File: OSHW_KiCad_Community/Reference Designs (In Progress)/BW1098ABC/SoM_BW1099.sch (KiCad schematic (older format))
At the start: 25 parts, among them J1 20021121-00010T1LF, J2 20021121-00010T1LF, J3 DF40HC(3.0)-100DS-0.4V_BW1099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, J4 20021121-00010T1LF, Q1 RE1C002UNTCL, Q2 RE1C002UNTCL, Q3 RE1C002UNTCL

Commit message: edits to abc
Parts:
- D1: value RED0603 -> RED
- D2, D3: value ORANGE0603 -> ORANGE
- R1, R2, R3, R4: value 1k 0402 -> 1k
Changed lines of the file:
@@
 AR Path="/5FF8D9B2/6009EFFA" Ref="D3"  Part="1"
 F 0 "D3" V 1939 7632 50  0000 R CNN
-F 1 "ORANGE0603" V 1848 7632 50  0000 R CNN
+F 1 "ORANGE" V 1848 7632 50  0000 R CNN
 F 2 "Diode_SMD:D_0603_1608Metric" H 1900 7750 50  0001 C CNN
 F 3 "~" H 1900 7750 50  0001 C CNN
@@
 AR Path="/5FF8D9B2/6009F000" Ref="R4"  Part="1"
 F 0 "R4" H 1968 7396 50  0000 L CNN
-F 1 "1k 0402" H 1968 7305 50  0000 L CNN
+F 1 "1k " H 1968 7305 50  0000 L CNN
 F 2 "Resistor_SMD:R_0402_1005Metric" H 1900 7350 50  0001 C CNN
 F 3 "~" H 1900 7350 50  0001 C CNN
@@
 AR Path="/5FF8D9B2/6009F015" Ref="D2"  Part="1"
 F 0 "D2" V 1889 5782 50  0000 R CNN
-F 1 "ORANGE0603" V 1798 5782 50  0000 R CNN
+F 1 "ORANGE" V 1798 5782 50  0000 R CNN
 F 2 "Diode_SMD:D_0603_1608Metric" H 1850 5900 50  0001 C CNN
 F 3 "~" H 1850 5900 50  0001 C CNN
@@
 AR Path="/5FF8D9B2/6009F01B" Ref="R3"  Part="1"
 F 0 "R3" H 1918 5546 50  0000 L CNN
-F 1 "1k 0402" H 1918 5455 50  0000 L CNN
+F 1 "1k" H 1918 5455 50  0000 L CNN
 F 2 "Resistor_SMD:R_0402_1005Metric" H 1850 5500 50  0001 C CNN
 F 3 "~" H 1850 5500 50  0001 C CNN
@@
 AR Path="/5FF8D9B2/6009F030" Ref="D1"  Part="1"
 F 0 "D1" V 1889 3482 50  0000 R CNN
-F 1 "RED0603" V 1798 3482 50  0000 R CNN
+F 1 "RED" V 1798 3482 50  0000 R CNN
 F 2 "Diode_SMD:D_0603_1608Metric" H 1850 3600 50  0001 C CNN
 F 3 "~" H 1850 3600 50  0001 C CNN
@@
 AR Path="/5FF8D9B2/6009F036" Ref="R2"  Part="1"
 F 0 "R2" H 1918 3246 50  0000 L CNN
-F 1 "1k 0402" H 1918 3155 50  0000 L CNN
+F 1 "1k" H 1918 3155 50  0000 L CNN
 F 2 "Resistor_SMD:R_0402_1005Metric" H 1850 3200 50  0001 C CNN
 F 3 "~" H 1850 3200 50  0001 C CNN
@@
 AR Path="/5FF8D9B2/6009F045" Ref="R1"  Part="1"
 F 0 "R1" H 1418 3146 50  0000 L CNN
-F 1 "1k 0402" H 1418 3055 50  0000 L CNN
+F 1 "1k" H 1418 3055 50  0000 L CNN
 F 2 "Resistor_SMD:R_0402_1005Metric" H 1350 3100 50  0001 C CNN
 F 3 "~" H 1350 3100 50  0001 C CNN

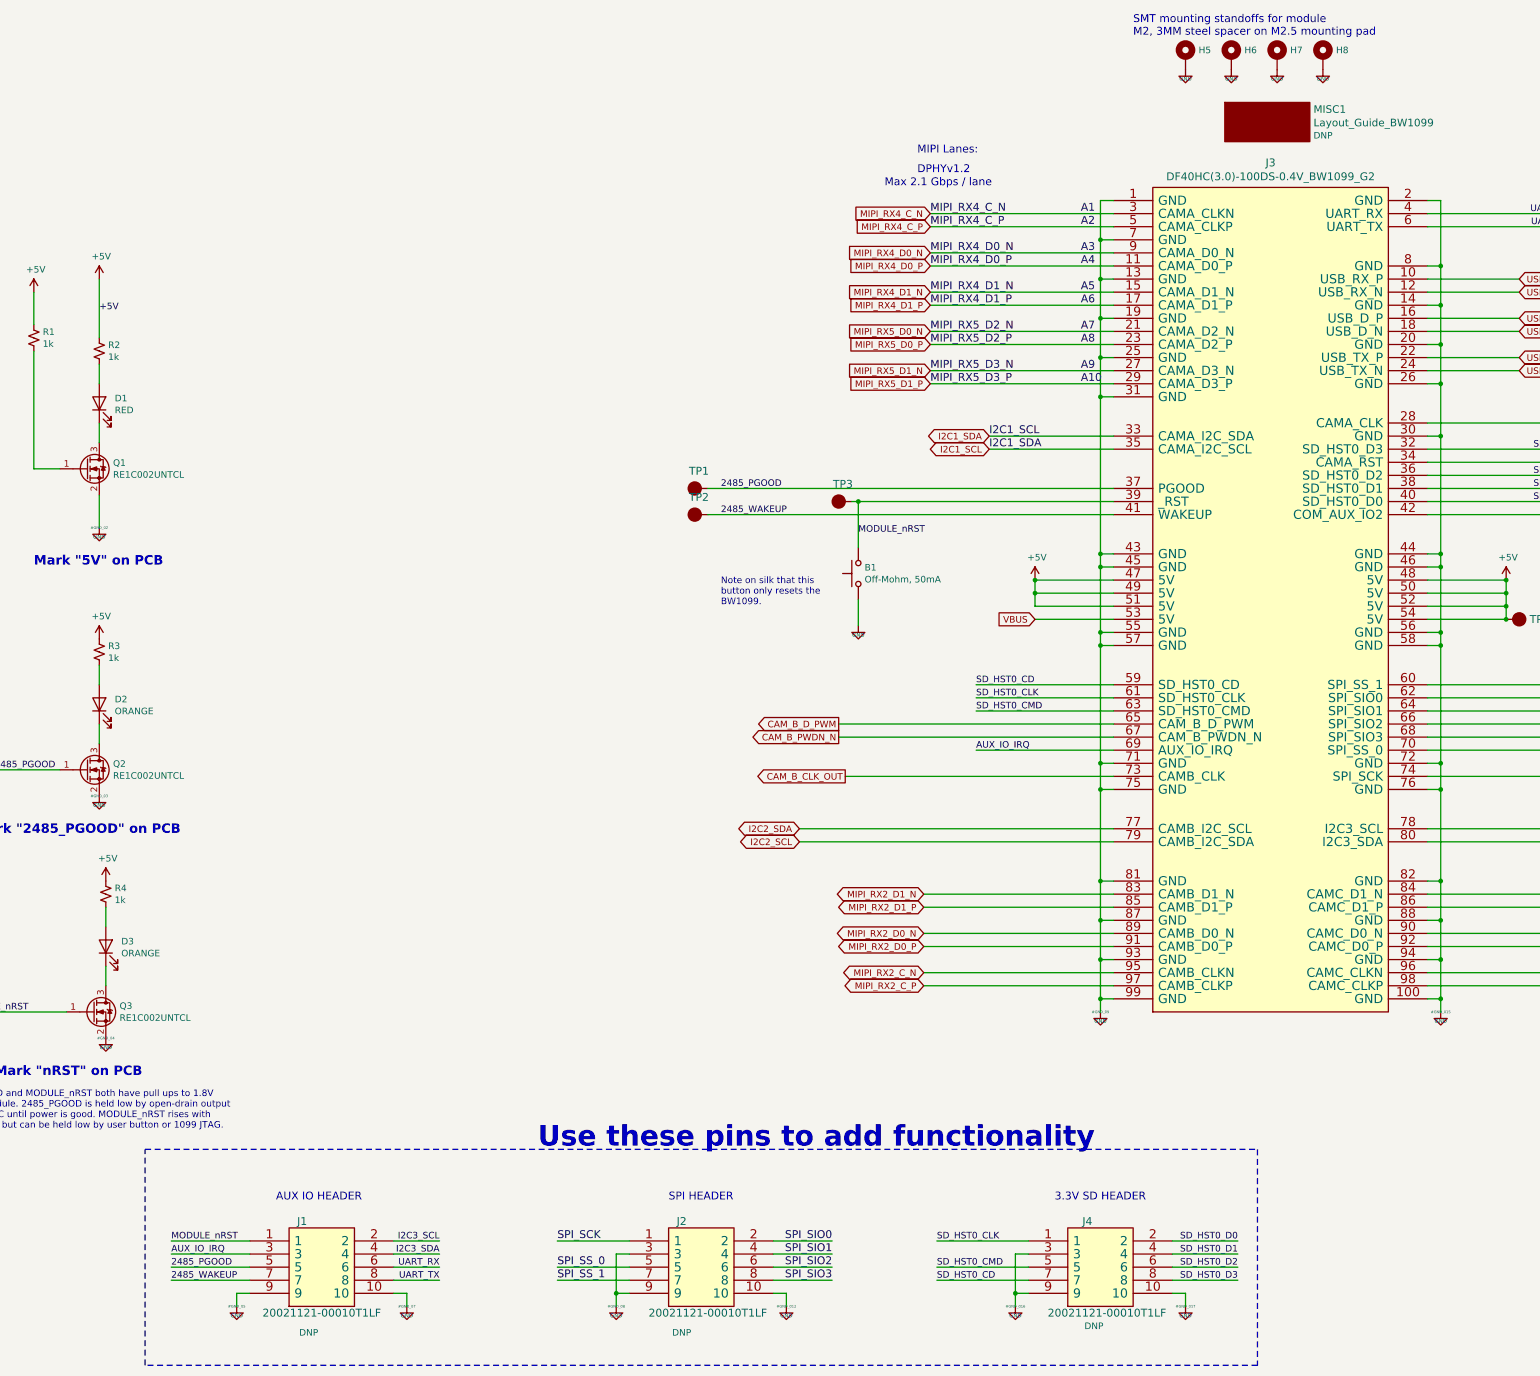
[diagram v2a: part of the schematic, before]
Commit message: added module mounts and started layout for abc
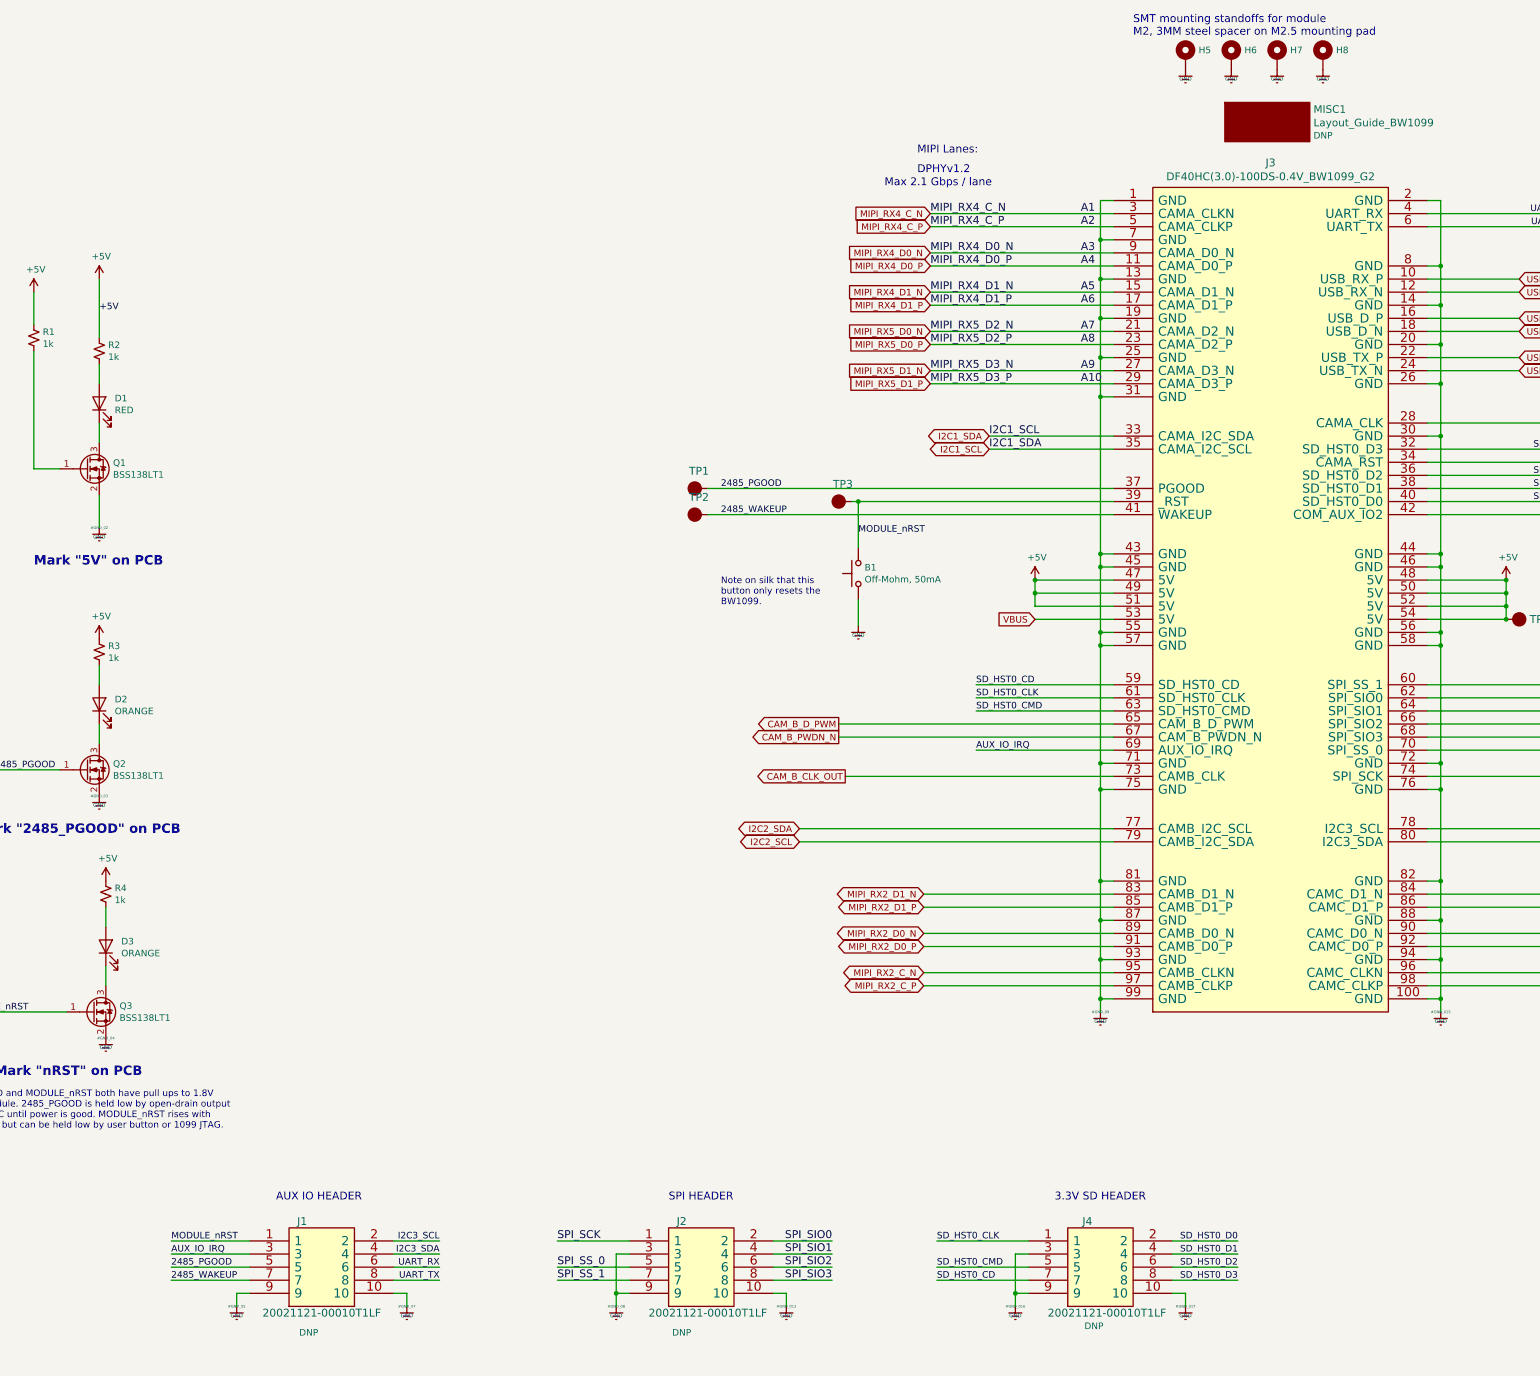
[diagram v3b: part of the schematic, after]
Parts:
- B1: footprint Luxonis_Kicad_Master:DTSM32NVTR -> Luxonis_KiCad_Master:DTSM32NVTR
- J3: footprint Luxonis_Kicad_Master:DF40HC(3.0)-100DS-0.4V(58) -> Luxonis_KiCad_Master:DF40HC(3.0)-100DS-0.4V(58)
- MISC1: footprint Luxonis_Kicad_Master:BW1099_Layout_Guide -> Luxonis_KiCad_Master:BW1099_Layout_Guide
- Q1, Q2, Q3: value RE1C002UNTCL -> BSS138LT1; footprint (none) -> Package_TO_SOT_SMD:SOT-23
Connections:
- net GND renamed Earth
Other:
- note removed: "Use these pins to add functionality"
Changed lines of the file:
@@
 $EndDescr
 $Comp
-L power:GND #GND_?
+L power:Earth #GND_?
 U 1 1 6009EE60
 P 12100 8250
@@
 SMT mounting standoffs for module\nM2, 3MM steel spacer on M2.5 mounting pad
 $Comp
-L power:GND #GND_?
+L power:Earth #GND_?
 U 1 1 6009EE67
 P 7650 5300
@@
 $EndComp
 $Comp
-L power:GND #GND_?
+L power:Earth #GND_?
 U 1 1 6009EE6D
 P 11200 1050
@@
 SPI_SIO3
 $Comp
-L power:GND #GND_?
+L power:Earth #GND_?
 U 1 1 6009EE7D
 P 4200 10500
@@
 $EndComp
 $Comp
-L power:GND #GND_?
+L power:Earth #GND_?
 U 1 1 6009EE83
 P 9500 8250
@@
 Mark "nRST" on PCB
 $Comp
-L power:GND #GND_?
+L power:Earth #GND_?
 U 1 1 6009EE8C
 P 1900 8450
@@
 $EndComp
 $Comp
-L power:GND #GND_?
+L power:Earth #GND_?
 U 1 1 6009EE92
 P 2900 10500
@@
 $EndComp
 $Comp
-L power:GND #GND_?
+L power:Earth #GND_?
 U 1 1 6009EE98
 P 5800 10500
@@
 $EndComp
 $Comp
-L power:GND #GND_?
+L power:Earth #GND_?
 U 1 1 6009EE9E
 P 7100 10500
@@
 $EndComp
 $Comp
-L power:GND #GND_?
+L power:Earth #GND_?
 U 1 1 6009EEA4
 P 8850 10500
@@
 $EndComp
 $Comp
-L power:GND #GND_?
+L power:Earth #GND_?
 U 1 1 6009EEAA
 P 10150 10500
@@
 $EndComp
 $Comp
-L power:GND #GND_?
+L power:Earth #GND_?
 U 1 1 6009EF80
 P 10850 1050
@@
 $EndComp
 $Comp
-L power:GND #GND_?
+L power:Earth #GND_?
 U 1 1 6009EF86
 P 10500 1050
@@
 $EndComp
 $Comp
-L power:GND #GND_?
+L power:Earth #GND_?
 U 1 1 6009EF8C
 P 10150 1050
@@
 F 0 "B1" V 7696 4852 50  0000 R CNN
 F 1 "Off-Mohm, 50mA" V 7605 4852 50  0000 R CNN
-F 2 "Luxonis_Kicad_Master:DTSM32NVTR" H 7650 5100 50  0001 C CNN
+F 2 "Luxonis_KiCad_Master:DTSM32NVTR" H 7650 5100 50  0001 C CNN
 F 3 "http://www.apem.com/int/index.php?controller=attachment&id_attachment=488" H 7650 5100 50  0001 C CNN
 	1    7650 4900
@@
 AR Path="/5FF8D9B2/6009F007" Ref="Q3"  Part="1"
 F 0 "Q3" H 2005 8296 50  0000 L CNN
-F 1 "RE1C002UNTCL" H 2005 8205 50  0000 L CNN
-F 2 "" H 2000 8350 50  0001 C CNN
+F 1 "BSS138LT1" H 2005 8205 50  0000 L CNN
+F 2 "Package_TO_SOT_SMD:SOT-23" H 2000 8350 50  0001 C CNN
 F 3 "~" H 1800 8250 50  0001 C CNN
 	1    1800 8250
@@
 	1900 8050 1900 7900
 $Comp
-L power:GND #GND_?
+L power:Earth #GND_?
 U 1 1 6009F00F
 P 1850 6600
@@
 AR Path="/5FF8D9B2/6009F022" Ref="Q2"  Part="1"
 F 0 "Q2" H 1955 6446 50  0000 L CNN
-F 1 "RE1C002UNTCL" H 1955 6355 50  0000 L CNN
-F 2 "" H 1950 6500 50  0001 C CNN
+F 1 "BSS138LT1" H 1955 6355 50  0000 L CNN
+F 2 "Package_TO_SOT_SMD:SOT-23" H 1950 6500 50  0001 C CNN
 F 3 "~" H 1750 6400 50  0001 C CNN
 	1    1750 6400
@@
 	1850 6200 1850 6050
 $Comp
-L power:GND #GND_?
+L power:Earth #GND_?
 U 1 1 6009F02A
 P 1850 4550
@@
 AR Path="/5FF8D9B2/6009F03D" Ref="Q1"  Part="1"
 F 0 "Q1" H 1955 4146 50  0000 L CNN
-F 1 "RE1C002UNTCL" H 1955 4055 50  0000 L CNN
-F 2 "" H 1950 4200 50  0001 C CNN
+F 1 "BSS138LT1" H 1955 4055 50  0000 L CNN
+F 2 "Package_TO_SOT_SMD:SOT-23" H 1950 4200 50  0001 C CNN
 F 3 "~" H 1750 4100 50  0001 C CNN
 	1    1750 4100
@@
 F 0 "J3" H 10800 2339 60  0000 C CNN
 F 1 "DF40HC(3.0)-100DS-0.4V_BW1099_G2" H 10800 2233 60  0000 C CNN
-F 2 "Luxonis_Kicad_Master:DF40HC(3.0)-100DS-0.4V(58)" H 9600 2050 60  0001 C CNN
+F 2 "Luxonis_KiCad_Master:DF40HC(3.0)-100DS-0.4V(58)" H 9600 2050 60  0001 C CNN
 F 3 "https://www.hirose.com/product/document?clcode=CL0684-4003-3-51&productname=DF40C-60DP-0.4V(51)&series=DF40&documenttype=Catalog&lang=en&documentid=D31649_en" H 9600 2050 60  0001 C CNN
 	1    9600 2050
@@
 F 0 "MISC1" H 11128 1547 58  0000 L CNN
 F 1 "Layout_Guide_BW1099" H 11128 1444 58  0000 L CNN
-F 2 "Luxonis_Kicad_Master:BW1099_Layout_Guide" H 10550 1850 58  0001 C CNN
+F 2 "Luxonis_KiCad_Master:BW1099_Layout_Guide" H 10550 1850 58  0001 C CNN
 F 3 "" H 10550 1850 58  0001 C CNN
 F 4 "DNP" H 11128 1347 50  0000 L CNN "Population"
@@
 Text GLabel 7500 6050 0    50   Output ~ 0
 CAM_B_D_PWM
-Wire Notes Line width 16 style solid rgb(0, 255, 0)
-	10700 10950 2200 10950
-Wire Notes Line width 16 style solid rgb(0, 255, 0)
-	2200 10950 2200 9300
-Wire Notes Line width 16 style solid rgb(0, 255, 0)
-	2200 9300 10700 9300
-Wire Notes Line width 16 style solid rgb(0, 255, 0)
-	10700 9300 10700 10950
-Text Notes 5200 9300 0    157  ~ 31
-Use these pins to add functionality
 $EndSCHEMATC

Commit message: abc board pcb work
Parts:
- removed J1, J4: 20021121-00010T1LF, symbol BW1098ABC-rescue:20021121-00010T1LF-depthAI_sch
- added J1, J4: Conn_02x05_Odd_Even, Connector_PinSocket_2.54mm:PinSocket_2x05_P2.54mm_Vertical, symbol Connector_Generic:Conn_02x05_Odd_Even
- J2: footprint (none) -> Connector_PinHeader_2.54mm:PinHeader_1x02_P2.54mm_Vertical
- R1, R2, R3, R4: footprint Resistor_SMD:R_0402_1005Metric -> Resistor_SMD:R_0603_1608Metric
- TP1, TP2, TP3, TP4, TP5: footprint TestPoint:TestPoint_Loop_D1.80mm_Drill1.0mm_Beaded -> TestPoint:TestPoint_Pad_1.0x1.0mm
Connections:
- net 2485_PGOOD: now also J1.5 (Pin_5)
- net 2485_WAKEUP: now also J1.7 (Pin_7)
- net AUX_IO_IRQ: now also J1.3 (Pin_3)
- net Earth: now also J1.10 (Pin_10), J1.9 (Pin_9), J4.10 (Pin_10), J4.3 (Pin_3), J4.9 (Pin_9)
- net I2C3_SCL: now also J1.2 (Pin_2)
- net I2C3_SDA: now also J1.4 (Pin_4)
- net MODULE_nRST: now also J1.1 (Pin_1)
- net SD_HST0_CD: now also J4.7 (Pin_7)
- net SD_HST0_CLK: now also J4.1 (Pin_1)
- net SD_HST0_CMD: now also J4.5 (Pin_5)
- net SD_HST0_D0: now also J4.2 (Pin_2)
- net SD_HST0_D1: now also J4.4 (Pin_4)
- net SD_HST0_D2: now also J4.6 (Pin_6)
- net SD_HST0_D3: now also J4.8 (Pin_8)
- net UART_RX: now also J1.6 (Pin_6)
- net UART_TX: now also J1.8 (Pin_8)
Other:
- moved on the sheet: J2

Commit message: layout
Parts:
- removed J2: 20021121-00010T1LF, Connector_PinHeader_2.54mm:PinHeader_1x02_P2.54mm_Vertical, symbol BW1098ABC-rescue:20021121-00010T1LF-depthAI_sch
- removed TP2, TP3: TEST_POINT, TestPoint:TestPoint_Pad_1.0x1.0mm, symbol BW1098ABC-rescue:TEST_POINT-depthAI_sch
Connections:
- net 2485_PGOOD: no longer J1.5 (Pin_5)
- net I2C1_SCL: no longer J3.33 (CAMA_I2C_SDA)
- net I2C3_SCL: no longer J1.2 (Pin_2)
- net I2C3_SDA: no longer J1.4 (Pin_4)
- net 2485_WAKEUP: no longer names the net of J3.41 (WAKEUP)
- net 2485_WAKEUP: no longer J1.7 (Pin_7)
- net MODULE_nRST renamed _RST
- net SPI_SS_0 renamed SPI_CS_0
- net SPI_SS_1 renamed SPI_CS_1
- new net I2C1_SDA: J3.33 (CAMA_I2C_SDA)
- no-connect marks 0 -> 1
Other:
- note added: "ALL PU/PD on SoM,\nSee Datasheet"
- note added: "DO NOT USE SPI0_CS_0 for \nanother peripheral IF \nyou are using the BW1099EMB\nit selects the nor flash"
- note added: "SPI0_SIO2&3 have 10k pullup on SoM"
- note removed: "SPI HEADER"
- moved on the sheet: B1, D1, D2, D3, H5, H6, H7, H8, J1, J3, J4, MISC1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

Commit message: ABC Updates
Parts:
- added D4, D5: RED, Diode_SMD:D_0603_1608Metric, symbol Device:LED
- added Q4, Q5: BSS138LT1, Package_TO_SOT_SMD:SOT-23, symbol Device:Q_NMOS_GSD
- added R29, R35: 100, Resistor_SMD:R_0603_1608Metric, symbol Device:R_Small_US
- added R30, R36: 1k, Resistor_SMD:R_0603_1608Metric, symbol Device:R_Small_US
- added R33, R34, R37: 10k, Resistor_SMD:R_0603_1608Metric, symbol Device:R_Small_US
- B1: footprint Luxonis_KiCad_Master:DTSM32NVTR -> depthABC:SW_PTS636_SM43J_SMTR_LFS; symbol Switch:SW_MEC_5G -> Switch:SW_SPST
- J1, J4: footprint Connector_PinSocket_2.54mm:PinSocket_2x05_P2.54mm_Vertical -> Connector_PinSocket_2.54mm:PinSocket_2x05_P2.54mm_Vertical_SMD
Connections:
- net +5V: now also R30.1, R36.1
- net Earth: now also Q4.2 (S), Q5.2 (S), R33.2, R34.2, R37.2; no longer B1.2 (A)
- net I2C3_SCL: now also J1.7 (Pin_7)
- net I2C3_SDA: now also J1.5 (Pin_5)
- net _RST: now also B1.2 (B); no longer B1.3 (B), B1.4 (B)
- net at Q1.1 (G), R1.2: now also R34.1
- net 1V8: now reaches J1.2 (Pin_2)
- net 1V8: now also J1.4 (Pin_4), R35.1
- net MIPI_RX5_D0_N renamed MIPI_RX5_D2_N
- net MIPI_RX5_D0_P renamed MIPI_RX5_D2_P
- net MIPI_RX5_D1_N renamed MIPI_RX5_D3_N
- net MIPI_RX5_D1_P renamed MIPI_RX5_D3_P
- new net: Q4.1 (G), R29.2, R33.1
- new net: D5.1 (K), Q5.3 (D)
- new net: D5.2 (A), R36.2
- new net: Q5.1 (G), R35.2, R37.1
- new net: D4.1 (K), Q4.3 (D)
- new net: D4.2 (A), R30.2
- new net +3V3: R29.1
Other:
- moved on the sheet: D1, D2, D3, J1, J3, MISC1, Q1, Q2, Q3, R1, R2, R3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

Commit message: prepping abc for protos
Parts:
- removed R33, R34, R37: 10k, Resistor_SMD:R_0603_1608Metric, symbol Device:R_Small_US
- added C3: 10uF, Capacitor_SMD:C_0603_1608Metric, symbol Device:C
- added TP3: ~, TestPoint:TestPoint_Plated_Hole_D2.0mm, symbol BW1098ABC-rescue:TEST_POINT-depthAI_sch
- B1: Link1 (none) -> https://www.digikey.com/en/products/detail/c-k/PTS636-SM43-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; MPN1 (none) -> PTS636
- H5, H6, H7, H8: Link1 (none) -> https://www.digikey.com/en/products/detail/9774030243R/732-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; MPN1 (none) -> 9774030243R; Population (none) -> NO POP
- J1, J4: MPN1 (none) -> 10132328-10011LF
- J3: value DF40HC(3.0)-100DS-0.4V_BW1099_G2 -> BW1099EMB_SoM; Link1 (none) -> https://www.hirose.com/product/document?clcode=CL0684-4003-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; MPN1 (none) -> DF40HC(3.0)-100DS-0.4V(58)
- MISC1: Population DNP -> NO POP
- Q1, Q2, Q3, Q4, Q5: value BSS138LT1 -> RK7002B; symbol Device:Q_NMOS_GSD -> Transistor_FET:DMG1012T; Link1 (none) -> https://www.digikey.com/en/products/detail/rohm-semiconduct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; Short Description (none) -> 2.5V Drive Nch MOSFET ESD Protection Diode
- R1, R2, R3, R30, R36: STANDARD (none) -> 1/10W 1%
- R29, R35: value 100 -> 1k; STANDARD (none) -> 1/10W 1%
- R4: value 1k -> 1k; STANDARD (none) -> 1/10W 1%
- TP1, TP4, TP5: value TEST_POINT -> ~; footprint TestPoint:TestPoint_Pad_1.0x1.0mm -> TestPoint:TestPoint_Plated_Hole_D2.0mm; Population (none) -> NO POP
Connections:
- net +5V: now also C3.2
- net Earth: now also C3.1
- net _RST: now also TP3.1 (P)

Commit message: abc updates
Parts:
- TP1, TP3, TP4, TP5: footprint TestPoint:TestPoint_Plated_Hole_D2.0mm -> TestPoint:TestPoint_Pad_D2.0mm
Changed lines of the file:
@@
 F 0 "TP1" V 1483 4468 60  0000 C CNN
 F 1 "~" H 1430 4415 60  0001 L CNN
-F 2 "TestPoint:TestPoint_Plated_Hole_D2.0mm" H 1350 4400 60  0001 C CNN
+F 2 "TestPoint:TestPoint_Pad_D2.0mm" H 1350 4400 60  0001 C CNN
 F 3 "~" H 1350 4400 60  0000 C CNN
 F 4 "~" H 1350 4400 50  0001 C CNN "Link1"
@@
 F 0 "TP4" V 7450 5580 60  0000 L CNN
 F 1 "~" H 7530 5415 60  0001 L CNN
-F 2 "TestPoint:TestPoint_Plated_Hole_D2.0mm" H 7450 5400 60  0001 C CNN
+F 2 "TestPoint:TestPoint_Pad_D2.0mm" H 7450 5400 60  0001 C CNN
 F 3 "~" H 7450 5400 60  0000 C CNN
 F 4 "~" H 7450 5400 50  0001 C CNN "Link1"
@@
 F 0 "TP5" H 8050 4750 60  0000 R CNN
 F 1 "~" H 8230 4615 60  0001 L CNN
-F 2 "TestPoint:TestPoint_Plated_Hole_D2.0mm" H 8150 4600 60  0001 C CNN
+F 2 "TestPoint:TestPoint_Pad_D2.0mm" H 8150 4600 60  0001 C CNN
 F 3 "~" H 8150 4600 60  0000 C CNN
 F 4 "~" H 8150 4600 50  0001 C CNN "Link1"
@@
 F 0 "TP3" V 3483 4568 60  0000 C CNN
 F 1 "~" H 3430 4515 60  0001 L CNN
-F 2 "TestPoint:TestPoint_Plated_Hole_D2.0mm" H 3350 4500 60  0001 C CNN
+F 2 "TestPoint:TestPoint_Pad_D2.0mm" H 3350 4500 60  0001 C CNN
 F 3 "~" H 3350 4500 60  0000 C CNN
 F 4 "~" H 3350 4500 50  0001 C CNN "Link1"
